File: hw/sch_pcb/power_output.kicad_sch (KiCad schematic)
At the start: 0 parts

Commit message: Edit schema
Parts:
- added C?: 10uF, Capacitor_SMD:C_0805_2012Metric, symbol Device:C
- added C? (x2): 47uF, Mlab_C:TantalC_SizeC_Reflow, symbol Device:C_Polarized_Small
- added C?: 47uF/6V3, Capacitor_SMD:C_0805_2012Metric, symbol Device:C
- added C?: 100nF, Capacitor_SMD:C_0805_2012Metric, symbol Device:C
- added C?: 10p, Capacitor_SMD:C_0805_2012Metric, symbol Device:C_Small
- added C?: 10uF, Capacitor_SMD:C_0805_2012Metric, symbol Device:C_Small
- added JP?: SolderJumper_2_Open, symbol Jumper:SolderJumper_2_Open
- added L?: DE1207-1, Mlab_L:DE1205-10, symbol Device:L_Small
- added P?: 1,1A, Mlab_F:1812, symbol untitled-eagle-import:POJISTKA_1812
- added R?: 10k, symbol Device:R
- added R?: 560k, Resistor_SMD:R_0805_2012Metric, symbol Device:R
- added R?: 100k, Resistor_SMD:R_0805_2012Metric, symbol Device:R
- added SV? (x6): MA03-2, untitled:MA03-2, symbol untitled-eagle-import:MA03-2
- added X?: TPS63060, Package_SON:Texas_S-PWSON-N10_ThermalVias, symbol Regulator_Switching:TPS63060
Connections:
- net battery_power: now also C?.1, C?.1, R?.1, X?.2 (VIN), X?.3 (EN)
- new net: JP?.2 (B), R?.2, X?.4 (PS/SYNC)
- new net: C?.1, C?.1, C?.2, R?.2, SV?.3 (K), SV?.3 (K), SV?.4 (K), SV?.4 (K), X?.9 (VOUT)
- new net: C?.1, R?.1, R?.2, X?.8 (FB)
- new net: C?.1, X?.6 (VAUX)
- new net: L?.1, X?.1 (L1)
- new net: L?.2, X?.10 (L2)
- new net GND: C?.1, C?.2, C?.2, C?.2, C?.2, C?.2, C?.2, JP?.1 (A), R?.1, SV?.1 (K), SV?.1 (K), SV?.2 (K), SV?.2 (K), SV?.5 (K), SV?.5 (K), SV?.6 (K), SV?.6 (K), X?.11 (PGND), X?.7 (GND)
- no-connect marks 0 -> 1
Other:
- note added: "For 3.3V"
- note added: "OUTPUT"

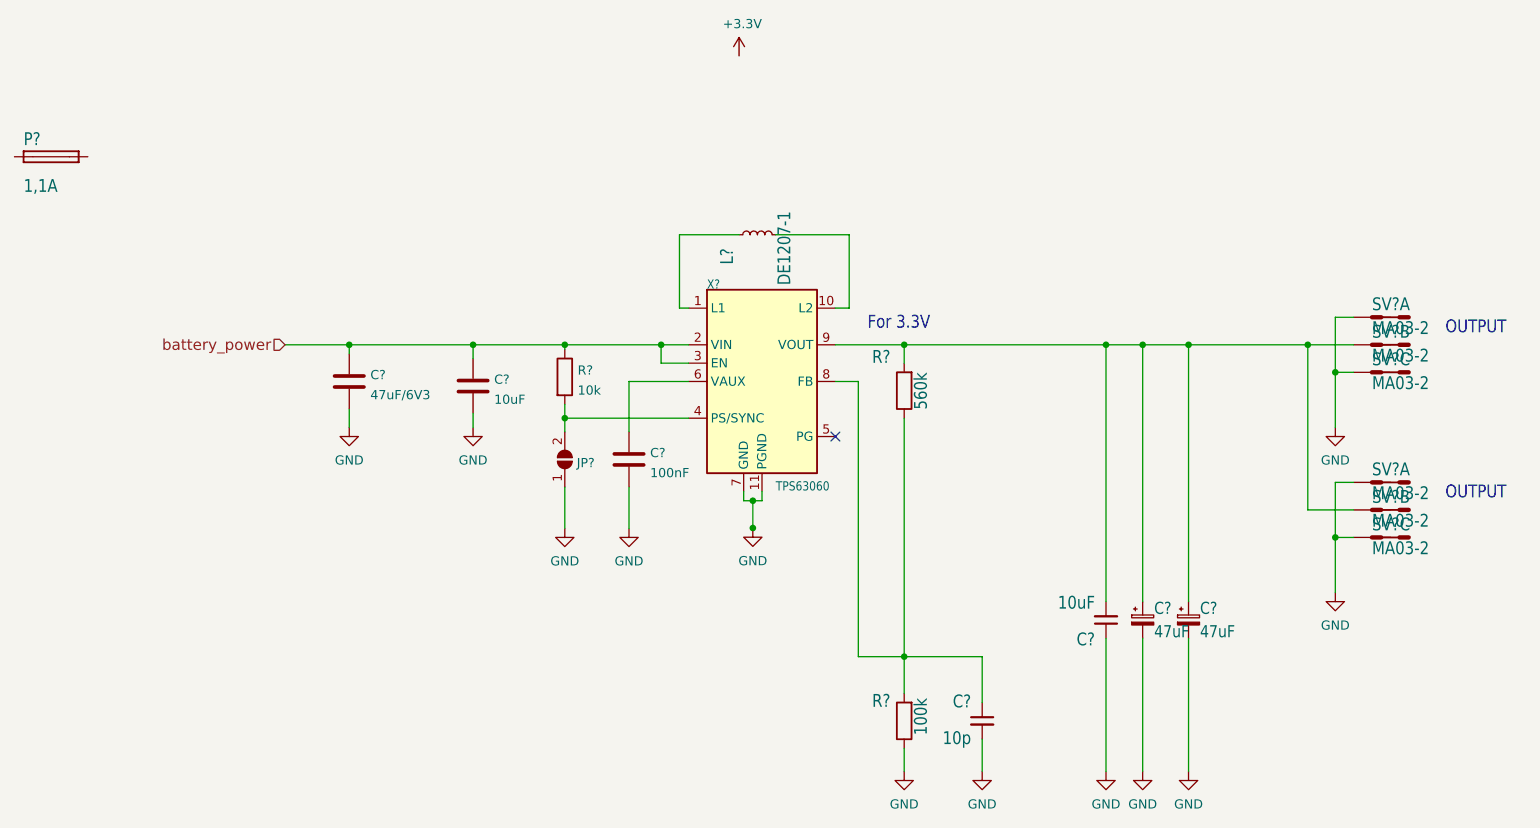
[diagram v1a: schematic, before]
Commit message: Update schematics: Adding datasheet Update title blocks Update pull-up value for CHARGE_CTRL signal.
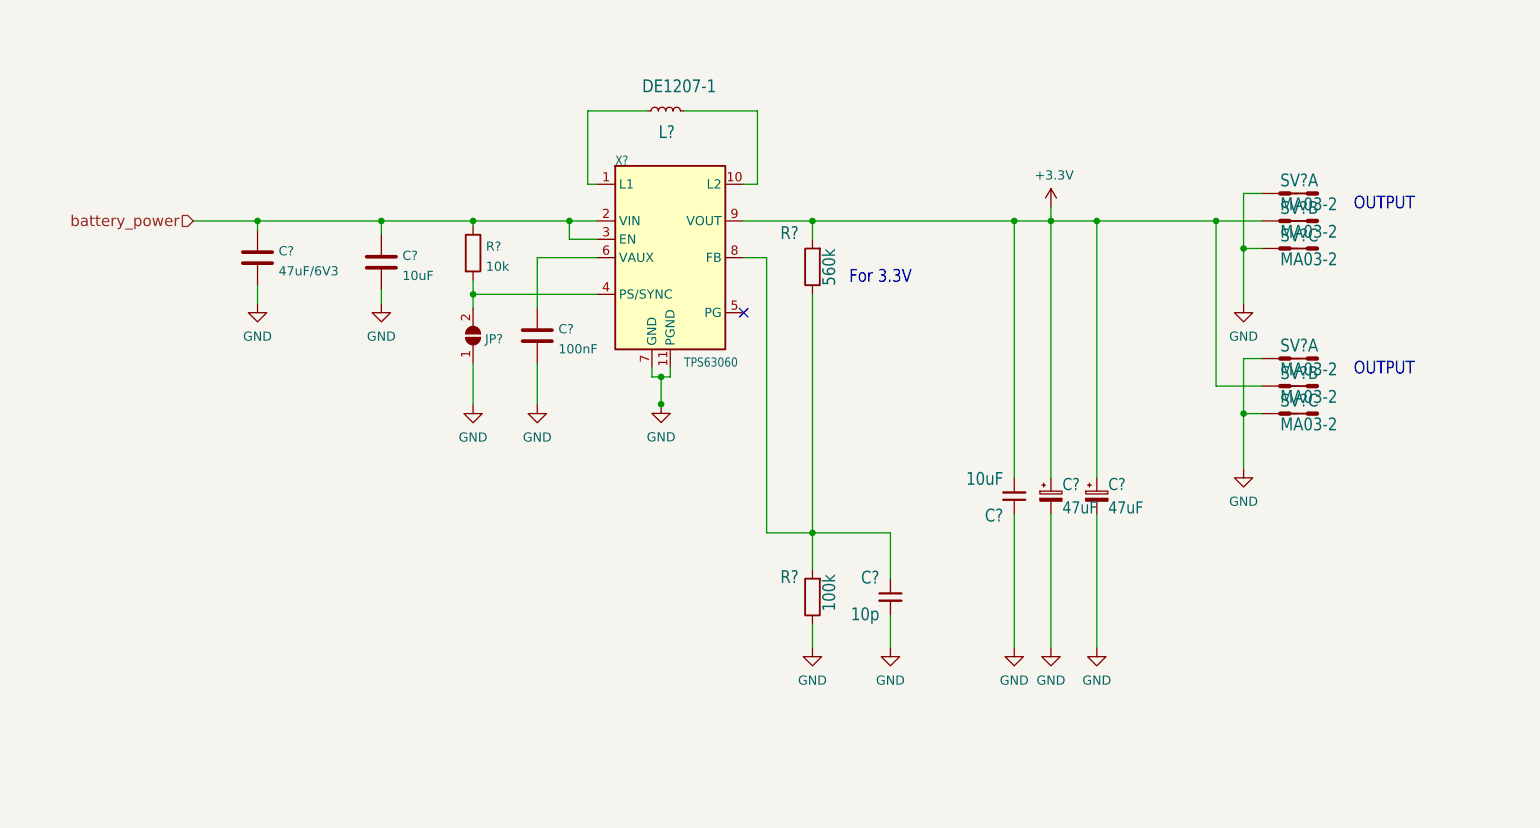
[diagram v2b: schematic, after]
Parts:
- removed P?: 1,1A, Mlab_F:1812, symbol untitled-eagle-import:POJISTKA_1812
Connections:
- net +3V3: now also C?.1, C?.1, C?.2, R?.2, SV?.3 (K), SV?.3 (K), SV?.4 (K), SV?.4 (K), X?.9 (VOUT)
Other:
- company: (none) -> MLAB.cz
- title: (none) -> SOLARMINIBAT01A
- moved on the sheet: C?, JP?, L?, R?, SV?A, SV?B, SV?C, X?

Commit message: Edit schema
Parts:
- removed C? (x2): 47uF, Mlab_C:TantalC_SizeC_Reflow, symbol Device:C_Polarized_Small
- removed C?: 10p, Capacitor_SMD:C_0805_2012Metric, symbol Device:C_Small
- removed C?: 10uF, Capacitor_SMD:C_0805_2012Metric, symbol Device:C_Small
- removed R?: 10k, symbol Device:R
- removed R?: 560k, Resistor_SMD:R_0805_2012Metric, symbol Device:R
- removed R?: 100k, Resistor_SMD:R_0805_2012Metric, symbol Device:R
- removed SV? (x6): MA03-2, untitled:MA03-2, symbol untitled-eagle-import:MA03-2
- added C19: 10pF, Capacitor_SMD:C_0805_2012Metric, symbol Device:C
- added C20: 10uF/6V3, Capacitor_SMD:C_0805_2012Metric, symbol Device:C
- added C21, C22: 47uF/6V3, Capacitor_SMD:C_0805_2012Metric, symbol Device:C
- added J5, J6: HEADER_2x03_PARALLEL, Mlab_Pin_Headers:Straight_2x03, symbol MLAB_HEADER:HEADER_2x03_PARALLEL
- added R24: 10k, Resistor_SMD:R_0805_2012Metric, symbol Device:R
- added R25: 560k, Resistor_SMD:R_0805_2012Metric, symbol Device:R
- added R26: 100k, Resistor_SMD:R_0805_2012Metric, symbol Device:R
- JP1: renamed from JP?; footprint (none) -> Jumper:SolderJumper-2_P1.3mm_Open_RoundedPad1.0x1.5mm
- gave numbers to parts that had none: 5
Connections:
- net +3V3: now also C20.1, C21.1, C22.1, J5.3, J5.4, J6.3, J6.4, R25.1
- net GND: now also C19.2, C20.2, C21.2, C22.2, J5.1, J5.2, J5.5, J5.6, J6.1, J6.2, J6.5, J6.6, R26.2
- net battery_power: now also R24.1
- net at JP1.2 (B), X1.4 (PS/SYNC): now also R24.2
- net at X1.8 (FB): now also C19.1, R25.2, R26.1
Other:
- note removed: "For 3.3V"
- note removed: "OUTPUT"

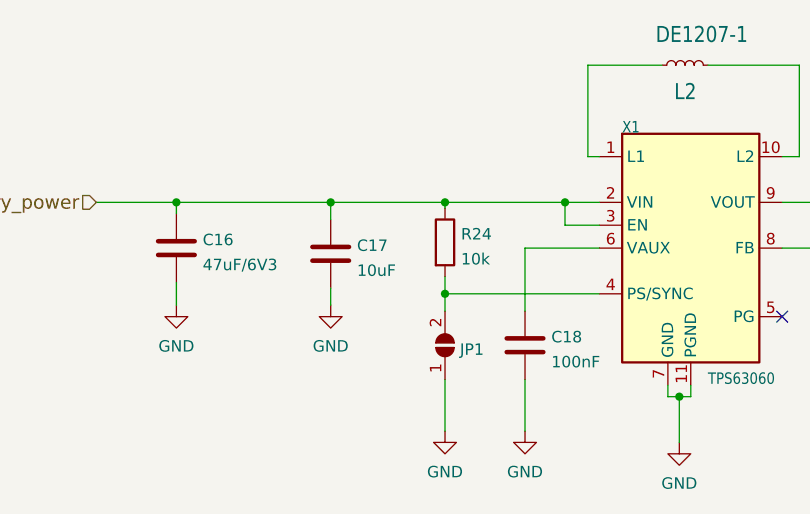
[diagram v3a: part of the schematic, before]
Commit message: Edit UST ID
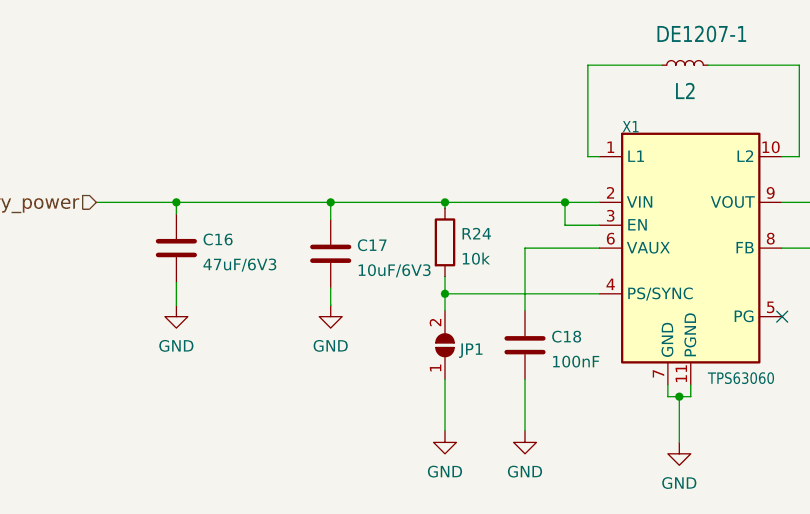
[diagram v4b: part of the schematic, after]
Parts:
- C16, C21, C22: UST_ID (none) -> 60d580ff1287500165f8595a
- C17: value 10uF -> 10uF/6V3; UST_ID (none) -> 5c70984712875079b91f8b53
- C18: UST_ID (none) -> 5c70984712875079b91f8b4c
- C19: UST_ID (none) -> 5c70984712875079b91f8b30
- C20: UST_ID (none) -> 5c70984712875079b91f8b53
- L2: UST_ID (none) -> 5c70984412875079b91f8823
- R24: UST_ID (none) -> 5c70984612875079b91f899f
- R25: UST_ID (none) -> 5c70984712875079b91f8aa6
- R26: UST_ID (none) -> 5c70984712875079b91f8a96
- X1: UST_ID (none) -> 5c70984612875079b91f89c2
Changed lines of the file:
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@@
+      (effects (font (size 1.27 1.27)) hide)
+    )
+    (property "UST_ID" "5c70984612875079b91f899f" (id 4) (at 100.965 73.66 0)
       (effects (font (size 1.27 1.27)) hide)
     )
@@
       (effects (font (size 1.27 1.27)) (justify left))
     )
-    (property "Value" "10uF" (id 1) (at 91.186 76.7966 0)
+    (property "Value" "10uF/6V3" (id 1) (at 91.186 76.7966 0)
       (effects (font (size 1.27 1.27)) (justify left))
     )
@@
       (effects (font (size 1.27 1.27)) hide)
     )
+    (property "UST_ID" "5c70984712875079b91f8b53" (id 4) (at 88.265 74.93 0)
+      (effects (font (size 1.27 1.27)) hide)
+    )
     (pin "1")
     (pin "2")
@@
     )
     (property "Datasheet" "~" (id 3) (at 158.75 87.63 0)
+      (effects (font (size 1.27 1.27)) hide)
+    )
+    (property "UST_ID" "5c70984712875079b91f8b30" (id 4) (at 158.75 87.63 0)
       (effects (font (size 1.27 1.27)) hide)
     )
@@
       (effects (font (size 1.27 1.27)) hide)
     )
+    (property "UST_ID" "60d580ff1287500165f8595a" (id 4) (at 71.12 74.295 0)
+      (effects (font (size 1.27 1.27)) hide)
+    )
     (pin "1")
     (pin "2")
@@
       (effects (font (size 1.27 1.27)) hide)
     )
+    (property "UST_ID" "5c70984712875079b91f8b4c" (id 4) (at 109.855 85.09 0)
+      (effects (font (size 1.27 1.27)) hide)
+    )
     (pin "1")
     (pin "2")
@@
     )
     (property "Datasheet" "~" (id 3) (at 147.955 75.565 0)
+      (effects (font (size 1.27 1.27)) hide)
+    )
+    (property "UST_ID" "5c70984712875079b91f8aa6" (id 4) (at 147.955 75.565 0)
       (effects (font (size 1.27 1.27)) hide)
     )
@@
     )
     (property "Datasheet" "http://www.ti.com/lit/ds/symlink/tps63060.pdf" (id 3) (at 128.27 74.295 0)
+      (effects (font (size 1.27 1.27)) hide)
+    )
+    (property "UST_ID" "5c70984612875079b91f89c2" (id 4) (at 128.27 74.295 0)
       (effects (font (size 1.27 1.27)) hide)
     )
@@
       (effects (font (size 1.27 1.27)) hide)
     )
+    (property "UST_ID" "60d580ff1287500165f8595a" (id 4) (at 182.245 81.28 0)
+      (effects (font (size 1.27 1.27)) hide)
+    )
     (pin "1")
     (pin "2")
@@
     )
     (property "Datasheet" "~" (id 3) (at 127.635 53.975 0)
+      (effects (font (size 1.27 1.27)) hide)
+    )
+    (property "UST_ID" "5c70984412875079b91f8823" (id 4) (at 127.635 53.975 0)
       (effects (font (size 1.27 1.27)) hide)
     )
@@
       (effects (font (size 1.27 1.27)) hide)
     )
+    (property "UST_ID" "5c70984712875079b91f8a96" (id 4) (at 147.955 88.9 0)
+      (effects (font (size 1.27 1.27)) hide)
+    )
     (pin "1")
     (pin "2")
@@
     )
     (property "Datasheet" "~" (id 3) (at 174.625 81.28 0)
+      (effects (font (size 1.27 1.27)) hide)
+    )
+    (property "UST_ID" "60d580ff1287500165f8595a" (id 4) (at 174.625 81.28 0)
       (effects (font (size 1.27 1.27)) hide)
     )
@@
       (effects (font (size 1.27 1.27)) hide)
     )
+    (property "UST_ID" "5c70984712875079b91f8b53" (id 4) (at 167.64 81.28 0)
+      (effects (font (size 1.27 1.27)) hide)
+    )

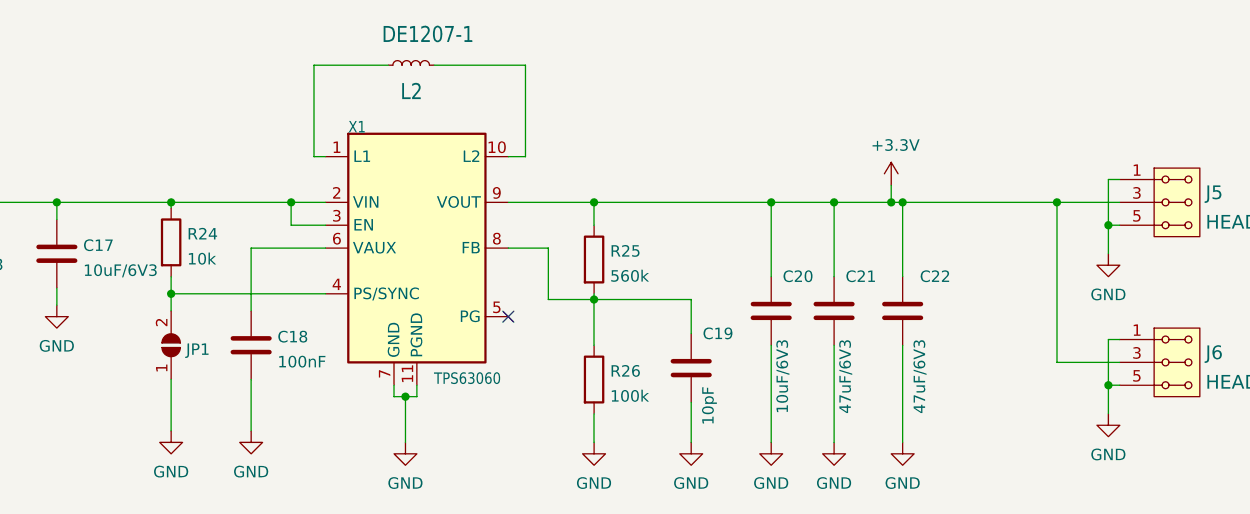
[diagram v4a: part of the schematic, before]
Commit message: Add datasheet to the used LTO cells. Improve documentation, update KiCAD project.
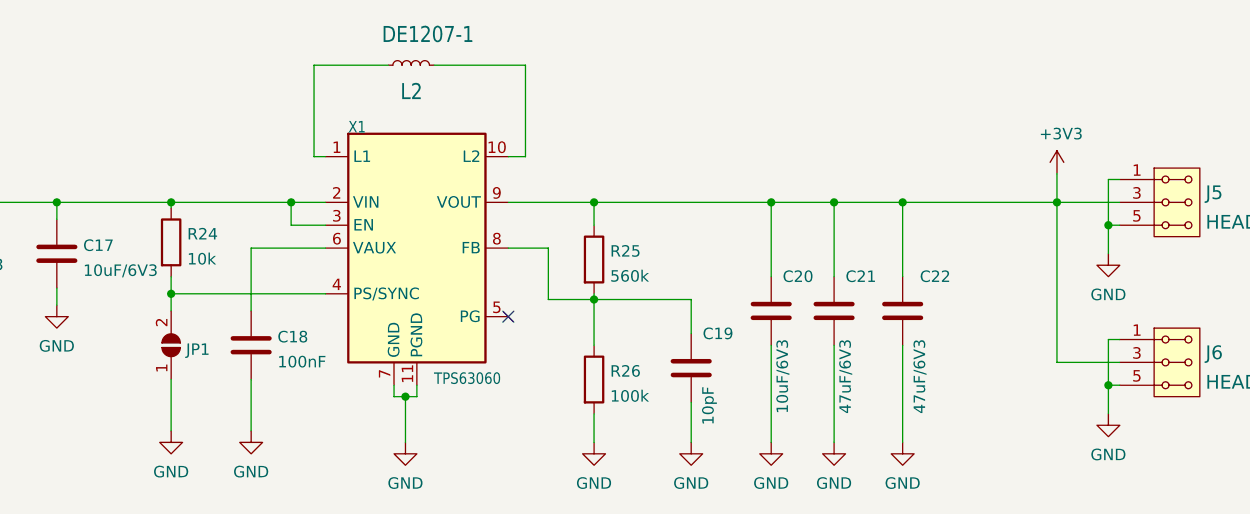
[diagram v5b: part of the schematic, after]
